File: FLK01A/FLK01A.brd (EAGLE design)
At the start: 30.5 x 30.5 mm, 32 parts, among them J1 M10SMD_MALE, J2 M10SMD_MALE, U1 LPC812TSSOP20, U2 EKMBTO5, U3 HTU21DSMD, U4 MMA8452Q, U5 VCNL4000, U6 MPL3115A2LGA8, U7 MMDT3904, Y1 12MHZ

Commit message: [pcb] clarify pin functions
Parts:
- R9: value 10k -> 1k
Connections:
- net PIO0_0 renamed ISP_RXD
- net PIO0_1 renamed RFM_SDI
- net PIO0_12 renamed !ISP_EN!
- net PIO0_13 renamed RFM_SDO
- net PIO0_14 renamed RFM_SEL
- net PIO0_17 renamed RFM_IRQ
- net PIO0_2 renamed SWDIO
- net PIO0_3 renamed SWCLK
- net PIO0_4 renamed ISP_TXD
- net PIO0_5 renamed !RESET!
- net PIO0_7 renamed RFM_SCK
- net PIO0_8 renamed QSPY_RXD
- net PIO0_9 renamed QSPY_TXD
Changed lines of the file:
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@@
 <attribute name="NAME" x="20.193" y="27.8765" size="0.4064" layer="25"/>
 </element>
-<element name="R9" library="SparkFun-Passives" package="0402-RES" value="10k" x="17.018" y="28.956" smashed="yes" rot="R270">
+<element name="R9" library="SparkFun-Passives" package="0402-RES" value="1k" x="17.018" y="28.956" smashed="yes" rot="R270">
 <attribute name="NAME" x="18.0975" y="28.575" size="0.4064" layer="25" rot="R90"/>
 </element>
@@
 <via x="17.018" y="3.048" extent="1-16" drill="0.4064" diameter="0.6096"/>
 </signal>
-<signal name="PIO0_17">
+<signal name="RFM_IRQ">
 <contactref element="U1" pad="1"/>
 <contactref element="J1" pad="1"/>
@@
 <wire x1="3.9628" y1="26.8228" x2="3.81" y2="26.67" width="0.254" layer="1"/>
 </signal>
-<signal name="PIO0_13">
+<signal name="RFM_SDO">
 <contactref element="U1" pad="2"/>
 <contactref element="J1" pad="2"/>
@@
 <wire x1="5.842" y1="24.13" x2="3.81" y2="24.13" width="0.254" layer="1"/>
 </signal>
-<signal name="PIO0_12">
+<signal name="!ISP_EN!">
 <contactref element="U1" pad="3"/>
 <contactref element="J1" pad="3"/>
@@
 <wire x1="5.842" y1="21.59" x2="3.81" y2="21.59" width="0.254" layer="1"/>
 </signal>
-<signal name="PIO0_5">
+<signal name="!RESET!">
 <contactref element="U1" pad="4"/>
 <contactref element="J1" pad="4"/>
@@
 <wire x1="11.938" y1="27.798" x2="11.43" y2="28.306" width="0.254" layer="1"/>
 </signal>
-<signal name="PIO0_4">
+<signal name="ISP_TXD">
 <contactref element="U1" pad="5"/>
 <contactref element="J1" pad="5"/>
@@
 <wire x1="14.224" y1="20.574" x2="12.192" y2="22.606" width="0.254" layer="1"/>
 </signal>
-<signal name="PIO0_3">
+<signal name="SWCLK">
 <contactref element="U1" pad="6"/>
 <contactref element="J1" pad="6"/>
@@
 <wire x1="5.842" y1="13.97" x2="3.81" y2="13.97" width="0.254" layer="1"/>
 </signal>
-<signal name="PIO0_2">
+<signal name="SWDIO">
 <contactref element="U1" pad="7"/>
 <contactref element="J1" pad="7"/>
@@
 <wire x1="6.35" y1="3.81" x2="3.81" y2="3.81" width="0.254" layer="1"/>
 </signal>
-<signal name="PIO0_14">
+<signal name="RFM_SEL">
 <contactref element="U1" pad="20"/>
 <contactref element="J2" pad="10"/>
@@
 <wire x1="26.5172" y1="26.8228" x2="26.67" y2="26.67" width="0.254" layer="1"/>
 </signal>
-<signal name="PIO0_0">
+<signal name="ISP_RXD">
 <contactref element="U1" pad="19"/>
 <contactref element="J2" pad="9"/>
@@
 <wire x1="14.986" y1="27.798" x2="15.494" y2="28.306" width="0.254" layer="1"/>
 </signal>
-<signal name="PIO0_7">
+<signal name="RFM_SCK">
 <contactref element="U1" pad="17"/>
 <contactref element="J2" pad="7"/>
@@
 <wire x1="23.114" y1="22.606" x2="23.114" y2="20.574" width="0.254" layer="1"/>
 </signal>
-<signal name="PIO0_9">
+<signal name="QSPY_TXD">
 <contactref element="U1" pad="13"/>
 <contactref element="Y1" pad="1"/>
@@
 <wire x1="24.638" y1="8.89" x2="26.67" y2="8.89" width="0.254" layer="1"/>
 </signal>
-<signal name="PIO0_1">
+<signal name="RFM_SDI">
 <contactref element="U1" pad="12"/>
 <contactref element="J2" pad="2"/>
@@
 <wire x1="6.238" y1="2.54" x2="6.35" y2="2.428" width="0.254" layer="1"/>
 </signal>
-<signal name="PIO0_8">
+<signal name="QSPY_RXD">
 <contactref element="U1" pad="14"/>
 <contactref element="Y1" pad="3"/>

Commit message: [pcb] re-assign sensor interrupt pins
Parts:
- removed R5: 100k, SparkFun-Passives:0402-RES
- removed U7: MMDT3904, SparkFun-DiscreteSemi:SOT363
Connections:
- net PIO0_15 renamed EKMB_INT
- removed net N$2: R4.1, R5.1, U7.5
- removed net N$4: R8.2, U4.11
- removed net N$5: R8.1, U7.2
- removed net PIO0_16: J1.10, U1.10, U6.6
- new net MMA_INT: J1.10, R8.2, U1.10, U4.11
- net GND: now also R4.1, R8.1; no longer R5.2, U7.1, U7.4
- net ISP_TXD: no longer U7.3, U7.6
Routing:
- net PIO0_16: track 24.1 -> 0.00 mm
- net MMA_INT: track 0.00 -> 21.9 mm
- net N$4: track 7.13 -> 0.00 mm
- net ISP_TXD: track 35.5 -> 29.8 mm
- net N$2: track 4.94 -> 0.00 mm
- net N$5: track 2.72 -> 0.00 mm
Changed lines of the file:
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@@
 <attribute name="NAME" x="17.907" y="7.112" size="0.4064" layer="25" font="vector"/>
-</element>
-<element name="U7" library="SparkFun-DiscreteSemi" package="SOT363" value="MMDT3904" x="18.034" y="10.668"/>
-<element name="R5" library="SparkFun-Passives" package="0402-RES" value="100k" x="20.574" y="11.684" smashed="yes" rot="R270">
-<attribute name="NAME" x="21.2725" y="12.065" size="0.4064" layer="25" rot="R270"/>
 </element>
 <element name="R8" library="SparkFun-Passives" package="0402-RES" value="100k" x="20.32" y="8.636" smashed="yes">
@@
 <contactref element="C5" pad="2"/>
 <contactref element="U4" pad="7"/>
-<contactref element="U7" pad="4"/>
-<contactref element="R5" pad="2"/>
-<contactref element="U7" pad="1"/>
 <contactref element="U5" pad="6"/>
 <contactref element="U5" pad="12"/>
@@
 <via x="15.748" y="1.524" extent="1-16" drill="0.4064" diameter="0.6096"/>
 <via x="17.018" y="3.048" extent="1-16" drill="0.4064" diameter="0.6096"/>
+<contactref element="R4" pad="1"/>
+<contactref element="R8" pad="1"/>
+<wire x1="20.308" y1="28.956" x2="29.464" y2="29.464" width="0" layer="19" extent="1-1"/>
+<wire x1="20.208" y1="23.368" x2="20.308" y2="28.956" width="0" layer="19" extent="1-1"/>
+<wire x1="20.828" y1="20.066" x2="20.208" y2="23.368" width="0" layer="19" extent="1-1"/>
+<wire x1="19.304" y1="20.066" x2="20.828" y2="20.066" width="0" layer="19" extent="1-1"/>
+<wire x1="16.875" y1="24.1812" x2="20.208" y2="23.368" width="0" layer="19" extent="1-1"/>
+<wire x1="15.494" y1="24.638" x2="16.4588" y2="24.1812" width="0" layer="19" extent="1-1"/>
+<wire x1="15.24" y1="19.304" x2="19.304" y2="20.066" width="0" layer="19" extent="1-1"/>
+<wire x1="12.558" y1="16.256" x2="15.24" y2="19.304" width="0" layer="19" extent="1-1"/>
+<wire x1="11.176" y1="15.24" x2="12.558" y2="16.256" width="0" layer="19" extent="1-1"/>
+<wire x1="13.443946875" y1="13.443946875" x2="11.176" y2="15.24" width="0" layer="19" extent="1-1"/>
+<wire x1="14.986" y1="10.302" x2="13.443946875" y2="13.443946875" width="0" layer="19" extent="1-1"/>
+<wire x1="17.272" y1="7.62" x2="14.986" y2="10.302" width="0" layer="19" extent="1-1"/>
+<wire x1="16.764" y1="6.492" x2="17.272" y2="7.62" width="0" layer="19" extent="1-1"/>
+<wire x1="14.732" y1="6.208" x2="16.764" y2="6.492" width="0" layer="19" extent="1-1"/>
+<wire x1="19.67" y1="8.636" x2="17.272" y2="7.62" width="0" layer="19" extent="1-1"/>
+<wire x1="20.574" y1="9.906" x2="19.67" y2="8.636" width="0" layer="19" extent="1-1"/>
+<wire x1="21.17" y1="7.366" x2="19.67" y2="8.636" width="0" layer="19" extent="1-1"/>
+<wire x1="20.579" y1="5.072" x2="21.17" y2="7.366" width="0" layer="19" extent="1-1"/>
+<wire x1="20.579" y1="4.072" x2="20.579" y2="5.072" width="0" layer="19" extent="1-1"/>
+<wire x1="19.304" y1="3.297" x2="20.579" y2="4.072" width="0" layer="19" extent="1-1"/>
+<wire x1="18.029" y1="3.572" x2="19.304" y2="3.297" width="0" layer="19" extent="1-1"/>
+<wire x1="17.018" y1="3.048" x2="18.029" y2="3.572" width="0" layer="19" extent="1-1"/>
+<wire x1="15.748" y1="1.524" x2="17.018" y2="3.048" width="0" layer="19" extent="1-1"/>
+<wire x1="14.454" y1="3.048" x2="15.748" y2="1.524" width="0" layer="19" extent="1-1"/>
+<wire x1="12.954" y1="3.048" x2="14.454" y2="3.048" width="0" layer="19" extent="1-1"/>
+<wire x1="22.86" y1="3.81" x2="20.579" y2="4.072" width="0" layer="19" extent="1-1"/>
+<wire x1="10.16" y1="1.89" x2="12.954" y2="3.048" width="0" layer="19" extent="1-1"/>
+<wire x1="19.954" y1="13.716" x2="20.574" y2="9.906" width="0" layer="19" extent="1-1"/>
+<wire x1="18.034" y1="15.24" x2="19.954" y2="13.716" width="0" layer="19" extent="1-1"/>
+<wire x1="6.35" y1="1.128" x2="10.16" y2="1.89" width="0" layer="19" extent="1-1"/>
+<wire x1="5.3285" y1="3.763" x2="6.35" y2="1.128" width="0" layer="19" extent="1-16"/>
+<wire x1="1.7835" y1="3.223" x2="5.3285" y2="3.763" width="0" layer="19" extent="16-16"/>
+<wire x1="2.398" y1="1.27" x2="1.7835" y2="3.223" width="0" layer="19" extent="1-16"/>
+<wire x1="1.016" y1="1.016" x2="2.398" y2="1.27" width="0" layer="19" extent="1-1"/>
+<wire x1="24.638" y1="17.78" x2="20.828" y2="20.066" width="0" layer="19" extent="1-1"/>
+<wire x1="26.67" y1="16.51" x2="24.638" y2="17.78" width="0" layer="19" extent="1-1"/>
+<wire x1="24.638" y1="15.24" x2="26.67" y2="16.51" width="0" layer="19" extent="1-1"/>
+<wire x1="29.21" y1="1.27" x2="22.86" y2="3.81" width="0" layer="19" extent="1-1"/>
+<wire x1="1.016" y1="29.464" x2="15.494" y2="24.638" width="0" layer="19" extent="1-1"/>
 </signal>
 <signal name="RFM_IRQ">
@@
 <wire x1="12.446" y1="24.892" x2="12.446" y2="27.798" width="0.254" layer="1"/>
 <wire x1="12.446" y1="27.798" x2="12.954" y2="28.306" width="0.254" layer="1"/>
-<contactref element="U7" pad="3"/>
-<contactref element="U7" pad="6"/>
-<wire x1="18.684" y1="9.868" x2="18.684" y2="10.526" width="0.254" layer="1"/>
-<wire x1="18.684" y1="10.526" x2="18.542" y2="10.668" width="0.254" layer="1"/>
-<wire x1="18.542" y1="10.668" x2="17.526" y2="10.668" width="0.254" layer="1"/>
-<wire x1="17.526" y1="10.668" x2="17.384" y2="10.81" width="0.254" layer="1"/>
-<wire x1="17.384" y1="10.81" x2="17.384" y2="11.478" width="0.254" layer="1"/>
 <via x="15.24" y="14.224" extent="1-16" drill="0.4064" diameter="0.6096"/>
 <wire x1="15.24" y1="14.224" x2="15.24" y2="16.256" width="0.254" layer="16"/>
@@
 <wire x1="12.192" y1="23.7244" x2="11.7352" y2="24.1812" width="0.254" layer="1"/>
 <wire x1="15.24" y1="14.224" x2="15.24" y2="13.622" width="0.254" layer="1"/>
-<wire x1="15.24" y1="13.622" x2="17.384" y2="11.478" width="0.254" layer="1"/>
 <wire x1="15.24" y1="16.256" x2="14.224" y2="17.526" width="0.254" layer="1"/>
 <wire x1="14.224" y1="17.526" x2="14.224" y2="20.574" width="0.254" layer="1"/>
@@
 <wire x1="11.438" y1="4.064" x2="11.454" y2="4.048" width="0.254" layer="1"/>
 </signal>
-<signal name="PIO0_16">
+<signal name="MMA_INT">
 <contactref element="U1" pad="10"/>
 <contactref element="J1" pad="10"/>
@@
 <wire x1="8.382" y1="11.684" x2="8.382" y2="9.906" width="0.254" layer="1"/>
 <wire x1="8.382" y1="9.906" x2="7.874" y2="9.398" width="0.254" layer="1"/>
-<contactref element="U6" pad="6"/>
-<wire x1="10.738" y1="10.023" x2="8.499" y2="10.023" width="0.254" layer="1"/>
 <wire x1="8.499" y1="10.023" x2="8.382" y2="9.906" width="0.254" layer="1"/>
 <wire x1="7.874" y1="9.398" x2="7.874" y2="8.128" width="0.254" layer="1"/>
@@
 <wire x1="7.366" y1="4.826" x2="6.35" y2="3.81" width="0.254" layer="1"/>
 <wire x1="6.35" y1="3.81" x2="3.81" y2="3.81" width="0.254" layer="1"/>
+<contactref element="U4" pad="11"/>
+<contactref element="R8" pad="2"/>
+<wire x1="20.579" y1="4.572" x2="20.97" y2="8.636" width="0" layer="19" extent="1-1"/>
+<wire x1="8.499" y1="10.023" x2="20.97" y2="8.636" width="0" layer="19" extent="1-1"/>
 </signal>
 <signal name="RFM_SEL">
@@
 <wire x1="24.638" y1="6.35" x2="26.67" y2="6.35" width="0.254" layer="1"/>
 </signal>
-<signal name="PIO0_15">
+<signal name="EKMB_INT">
 <contactref element="U1" pad="11"/>
 <contactref element="J2" pad="1"/>
@@
 <wire x1="16.884" y1="5.072" x2="16.764" y2="5.192" width="0.254" layer="1"/>
 </signal>
-<signal name="N$2">
-<contactref element="R4" pad="1"/>
-<contactref element="U7" pad="5"/>
-<contactref element="R5" pad="1"/>
-<contactref element="R5" pad="1"/>
-<wire x1="19.954" y1="13.716" x2="19.954" y2="13.096" width="0.254" layer="1"/>
-<wire x1="19.954" y1="13.096" x2="19.304" y2="12.446" width="0.254" layer="1"/>
-<wire x1="19.304" y1="12.446" x2="18.288" y2="12.446" width="0.254" layer="1"/>
-<wire x1="18.288" y1="12.446" x2="18.034" y2="12.192" width="0.254" layer="1"/>
-<wire x1="18.034" y1="12.192" x2="18.034" y2="11.478" width="0.254" layer="1"/>
-<wire x1="19.304" y1="12.446" x2="20.462" y2="12.446" width="0.254" layer="1"/>
-<wire x1="20.462" y1="12.446" x2="20.574" y2="12.334" width="0.254" layer="1"/>
-</signal>
-<signal name="N$4">
-<contactref element="U4" pad="11"/>
-<contactref element="R8" pad="2"/>
-<wire x1="22.098" y1="7.112" x2="22.606" y2="6.604" width="0.254" layer="1"/>
-<wire x1="22.098" y1="7.112" x2="22.098" y2="8.382" width="0.254" layer="1"/>
-<wire x1="22.606" y1="6.604" x2="22.606" y2="4.826" width="0.254" layer="1"/>
-<wire x1="22.098" y1="8.382" x2="21.844" y2="8.636" width="0.254" layer="1"/>
-<wire x1="21.844" y1="8.636" x2="20.97" y2="8.636" width="0.254" layer="1"/>
-<wire x1="20.579" y1="4.572" x2="22.352" y2="4.572" width="0.254" layer="1"/>
-<wire x1="22.352" y1="4.572" x2="22.606" y2="4.826" width="0.254" layer="1"/>
-</signal>
-<signal name="N$5">
-<contactref element="R8" pad="1"/>
-<contactref element="U7" pad="2"/>
-<wire x1="18.034" y1="9.868" x2="18.034" y2="8.89" width="0.254" layer="1"/>
-<wire x1="18.034" y1="8.89" x2="18.288" y2="8.636" width="0.254" layer="1"/>
-<wire x1="18.288" y1="8.636" x2="19.67" y2="8.636" width="0.254" layer="1"/>
-</signal>
 <signal name="N$1">

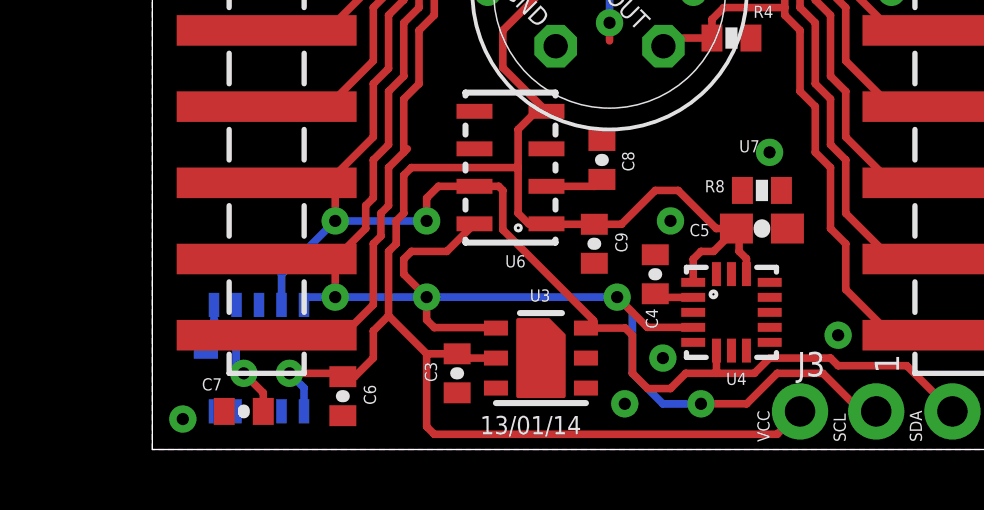
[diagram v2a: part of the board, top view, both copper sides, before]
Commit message: [pcb] increase C5 size from 0603 to 0805
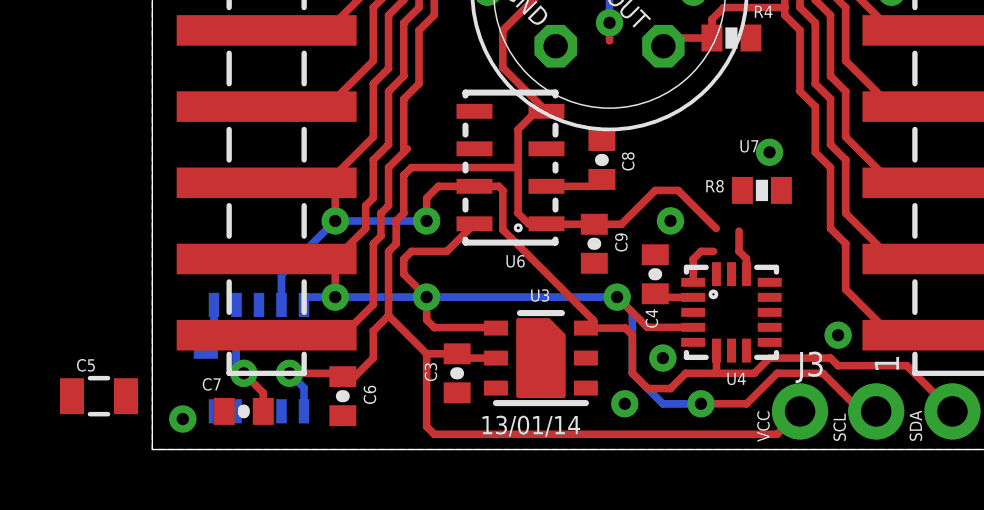
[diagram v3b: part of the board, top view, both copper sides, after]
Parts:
- C5: value 4.7u -> 4.7uF; device flukso:0603-CAP -> flukso:0805
- moved C5 22.8 mm to (-1.78, 1.78)
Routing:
- net 3.3V: track 103.6 -> 101.6 mm
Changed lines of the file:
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@@
 <attribute name="NAME" x="16.4465" y="4.699" size="0.4064" layer="25" rot="R270"/>
-</element>
-<element name="C5" library="flukso" package="0603-CAP" value="4.7u" x="20.32" y="7.366" smashed="yes">
-<attribute name="NAME" x="17.907" y="7.112" size="0.4064" layer="25" font="vector"/>
 </element>
 <element name="R8" library="SparkFun-Passives" package="0402-RES" value="100k" x="20.32" y="8.636" smashed="yes">
@@
 <attribute name="VALUE" x="30.48" y="4.445" size="1.27" layer="27" rot="R180"/>
 </element>
+<element name="C5" library="flukso" package="0805" value="4.7uF" x="-1.778" y="1.778"/>
 </elements>
 <signals>
@@
 <contactref element="U4" pad="5"/>
 <contactref element="C4" pad="2"/>
-<contactref element="C5" pad="2"/>
 <contactref element="U4" pad="7"/>
 <contactref element="U5" pad="6"/>
@@
 <contactref element="R4" pad="1"/>
 <contactref element="R8" pad="1"/>
+<contactref element="C5" pad="2"/>
 <wire x1="20.308" y1="28.956" x2="29.464" y2="29.464" width="0" layer="19" extent="1-1"/>
 <wire x1="20.208" y1="23.368" x2="20.308" y2="28.956" width="0" layer="19" extent="1-1"/>
@@
 <wire x1="19.67" y1="8.636" x2="17.272" y2="7.62" width="0" layer="19" extent="1-1"/>
 <wire x1="20.574" y1="9.906" x2="19.67" y2="8.636" width="0" layer="19" extent="1-1"/>
-<wire x1="21.17" y1="7.366" x2="19.67" y2="8.636" width="0" layer="19" extent="1-1"/>
-<wire x1="20.579" y1="5.072" x2="21.17" y2="7.366" width="0" layer="19" extent="1-1"/>
-<wire x1="20.579" y1="4.072" x2="20.579" y2="5.072" width="0" layer="19" extent="1-1"/>
-<wire x1="19.304" y1="3.297" x2="20.579" y2="4.072" width="0" layer="19" extent="1-1"/>
-<wire x1="18.029" y1="3.572" x2="19.304" y2="3.297" width="0" layer="19" extent="1-1"/>
-<wire x1="17.018" y1="3.048" x2="18.029" y2="3.572" width="0" layer="19" extent="1-1"/>
-<wire x1="15.748" y1="1.524" x2="17.018" y2="3.048" width="0" layer="19" extent="1-1"/>
-<wire x1="14.454" y1="3.048" x2="15.748" y2="1.524" width="0" layer="19" extent="1-1"/>
+<wire x1="14.454" y1="3.048" x2="14.732" y2="6.208" width="0" layer="19" extent="1-1"/>
 <wire x1="12.954" y1="3.048" x2="14.454" y2="3.048" width="0" layer="19" extent="1-1"/>
+<wire x1="15.748" y1="1.524" x2="14.454" y2="3.048" width="0" layer="19" extent="1-1"/>
+<wire x1="17.018" y1="3.048" x2="15.748" y2="1.524" width="0" layer="19" extent="1-1"/>
+<wire x1="18.029" y1="3.572" x2="17.018" y2="3.048" width="0" layer="19" extent="1-1"/>
+<wire x1="19.304" y1="3.297" x2="18.029" y2="3.572" width="0" layer="19" extent="1-1"/>
+<wire x1="20.579" y1="4.072" x2="19.304" y2="3.297" width="0" layer="19" extent="1-1"/>
+<wire x1="20.579" y1="5.072" x2="20.579" y2="4.072" width="0" layer="19" extent="1-1"/>
 <wire x1="22.86" y1="3.81" x2="20.579" y2="4.072" width="0" layer="19" extent="1-1"/>
 <wire x1="10.16" y1="1.89" x2="12.954" y2="3.048" width="0" layer="19" extent="1-1"/>
@@
 <wire x1="2.398" y1="1.27" x2="1.7835" y2="3.223" width="0" layer="19" extent="1-16"/>
 <wire x1="1.016" y1="1.016" x2="2.398" y2="1.27" width="0" layer="19" extent="1-1"/>
+<wire x1="-0.878" y1="1.778" x2="1.016" y2="1.016" width="0" layer="19" extent="1-1"/>
 <wire x1="24.638" y1="17.78" x2="20.828" y2="20.066" width="0" layer="19" extent="1-1"/>
 <wire x1="26.67" y1="16.51" x2="24.638" y2="17.78" width="0" layer="19" extent="1-1"/>
@@
 <contactref element="U4" pad="14"/>
 <contactref element="U4" pad="1"/>
-<contactref element="C5" pad="1"/>
 <contactref element="U5" pad="7"/>
 <contactref element="C6" pad="1"/>
@@
 <wire x1="13.858" y1="16.256" x2="13.858" y2="15.382" width="0.254" layer="1"/>
 <wire x1="13.858" y1="15.382" x2="13.716" y2="15.24" width="0.254" layer="1"/>
-<wire x1="19.558" y1="7.366" x2="19.47" y2="7.366" width="0.254" layer="1"/>
 <wire x1="17.526" y1="8.636" x2="18.796" y2="7.366" width="0.254" layer="1"/>
-<wire x1="18.796" y1="7.366" x2="19.47" y2="7.366" width="0.254" layer="1"/>
 <contactref element="J3" pad="4"/>
 <wire x1="21.59" y1="1.27" x2="20.828" y2="0.508" width="0.254" layer="1"/>
@@
 <wire x1="19.804" y1="6.358" x2="19.558" y2="6.604" width="0.254" layer="1"/>
 <wire x1="19.558" y1="6.604" x2="19.558" y2="7.278" width="0.254" layer="1"/>
-<wire x1="19.558" y1="7.278" x2="19.47" y2="7.366" width="0.254" layer="1"/>
 <wire x1="18.029" y1="5.572" x2="18.029" y2="6.345" width="0.254" layer="1"/>
 <wire x1="18.029" y1="6.345" x2="18.288" y2="6.604" width="0.254" layer="1"/>
 <wire x1="18.288" y1="6.604" x2="18.708" y2="6.604" width="0.254" layer="1"/>
-<wire x1="18.708" y1="6.604" x2="19.47" y2="7.366" width="0.254" layer="1"/>
 <wire x1="7.874" y1="6.604" x2="7.874" y2="4.46" width="0.254" layer="1"/>
 <wire x1="7.874" y1="4.46" x2="9.144" y2="3.19" width="0.254" layer="1"/>
@@
 <wire x1="4.572" y1="2.54" x2="6.238" y2="2.54" width="0.254" layer="1"/>
 <wire x1="6.238" y1="2.54" x2="6.35" y2="2.428" width="0.254" layer="1"/>
+<contactref element="C5" pad="1"/>
+<wire x1="18.796" y1="7.366" x2="19.558" y2="7.278" width="0" layer="19" extent="1-1"/>
+<wire x1="18.708" y1="6.604" x2="18.796" y2="7.366" width="0" layer="19" extent="1-1"/>
+<wire x1="-2.678" y1="1.778" x2="4.572" y2="2.54" width="0" layer="19" extent="1-1"/>
 </signal>
 <signal name="QSPY_RXD">

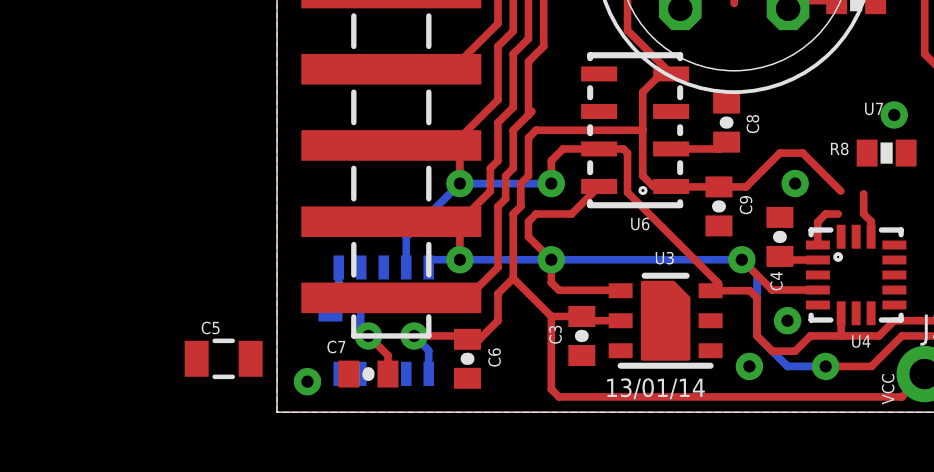
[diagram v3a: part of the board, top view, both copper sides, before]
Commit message: [pcb] correct HTU21D footprint
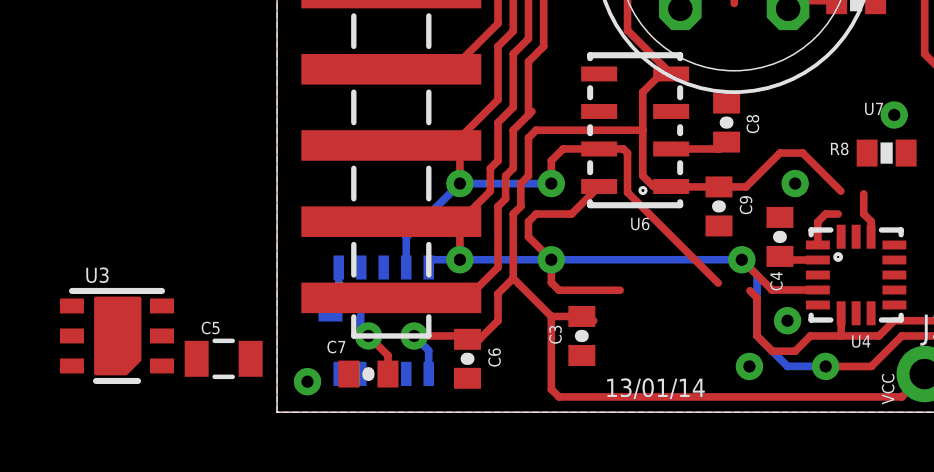
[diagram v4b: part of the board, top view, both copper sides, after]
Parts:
- U3: device flukso:HTU21D -> SparkFun-Sensors:HTU21D
- moved U3 18.3 mm to (-5.33, 2.54), turned to 0 degrees
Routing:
- net I2C0_SDA: track 55.2 -> 53.5 mm
- net 3.3V: track 101.6 -> 100.7 mm
